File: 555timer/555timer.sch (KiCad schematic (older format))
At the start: 6 parts, among them SW1 SW_Push, U1 NE555

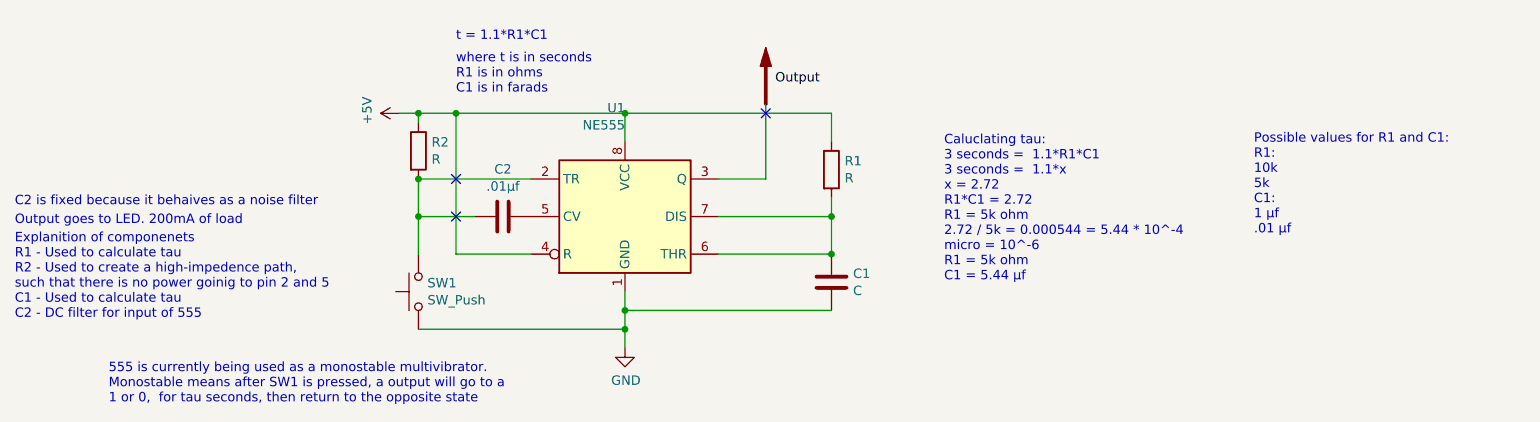
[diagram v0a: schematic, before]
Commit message: :recycle: Removing noise from schematic
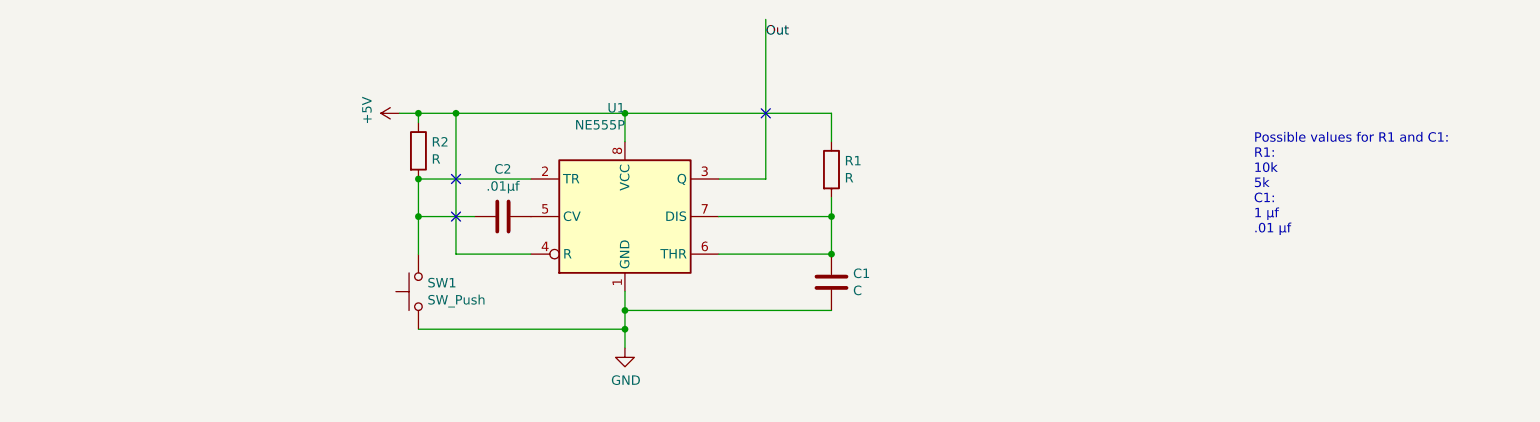
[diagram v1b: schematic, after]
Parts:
- U1: value NE555 -> NE555P
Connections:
- net labels added: Out
- net labels removed: Output
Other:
- note removed: "555 is currently being used as a monostable multivibrator. \nMonostable means after SW1 is pressed, a output will go to a\n1 or 0, for tau seconds, then return to the opposite state"
- note removed: "C2 is fixed because it behaives as a noise filter"
- note removed: "Caluclating tau:\n3 seconds = 1.1*R1*C1\n3 seconds = 1.1*x\nx = 2.72\nR1*C1 = 2.72\nR1 = 5k ohm\n2.72 / 5k = 0.000544 = 5.44 * 10^-4\nmicro = 10^-6\nR1 = 5k ohm\nC1 = 5.44 μf\n"
- note removed: "Explanition of componenets\nR1 - Used to calculate tau\nR2 - Used to create a high-impedence path,\nsuch that there is no power goinig to pin 2 and 5 \nC1 - Used to calculate tau\nC2 - DC filter for input of 555\n"
- note removed: "Output goes to LED. 200mA of load"
- note removed: "t = 1.1*R1*C1\n\n"
- note removed: "where t is in seconds\nR1 is in ohms\nC1 is in farads"
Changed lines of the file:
@@
 P 5000 3800
 F 0 "U1" H 5000 4378 50  0000 R CNN
-F 1 "NE555" H 5000 4287 50  0000 R CNN
+F 1 "NE555P" H 5000 4287 50  0000 R CNN
 F 2 "" H 5000 3800 50  0001 C CNN
 F 3 "http://www.ti.com/lit/ds/symlink/ne555.pdf" H 5000 3800 50  0001 C CNN
@@
 	6100 4000 5500 4000
 Connection ~ 6100 3800
-$Comp
-L Graphic:SYM_Arrow_Large #SYM?
-U 1 1 5C9155A3
-P 5750 3050
-F 0 "#SYM?" H 5750 3140 50  0001 C CNN
-F 1 "SYM_Arrow_Large" H 5750 2970 50  0001 C CNN
-F 2 "" H 5750 3050 50  0001 C CNN
-F 3 "~" H 5750 3050 50  0001 C CNN
-	1    5750 3050
-	0    -1   -1   0
-$EndComp
 Wire Wire Line
 	5500 3600 5750 3600
-Text Label 5800 3100 0    50   ~ 0
-Output
 $Comp
 L Device:R R2
@@
 Wire Wire Line
 	5000 3250 6100 3250
-Wire Wire Line
-	5750 3600 5750 3200
 Wire Wire Line
 	3900 3600 3900 3800
@@
 Wire Wire Line
 	3900 3800 3900 4000
-Text Notes 4100 2950 0    50   ~ 0
-t = 1.1*R1*C1\n\n
-Text Notes 4100 3150 0    50   ~ 0
-where t is in seconds\nR1 is in ohms\nC1 is in farads
-Text Notes 1750 3750 0    50   ~ 0
-C2 is fixed because it behaives as a noise filter
-Text Notes 1750 3850 0    50   ~ 0
-Output goes to LED. 200mA of load
-Text Notes 1750 4350 0    50   ~ 0
-Explanition of componenets\nR1 - Used to calculate tau\nR2 - Used to create a high-impedence path,\nsuch that there is no power goinig to pin 2 and 5 \nC1 - Used to calculate tau\nC2 - DC filter for input of 555\n
 NoConn ~ 5750 3250
 NoConn ~ 4100 3600
 NoConn ~ 4100 3800
-Text Notes 2250 4800 0    50   ~ 0
-555 is currently being used as a monostable multivibrator. \nMonostable means after SW1 is pressed, a output will go to a\n1 or 0,  for tau seconds, then return to the opposite state
-Text Notes 6700 4150 0    50   ~ 0
-Caluclating tau:\n3 seconds =  1.1*R1*C1\n3 seconds =  1.1*x\nx = 2.72\nR1*C1 = 2.72\nR1 = 5k ohm\n2.72 / 5k = 0.000544 = 5.44 * 10^-4\nmicro = 10^-6\nR1 = 5k ohm\nC1 = 5.44 μf\n
 Text Notes 8350 3900 0    50   ~ 0
 Possible values for R1 and C1:\nR1:\n10k\n5k\nC1:\n1 μf\n.01 μf
+Wire Wire Line
+	5750 2750 5750 3600
+Text Label 5750 2850 0    50   ~ 0
+Out
 $EndSCHEMATC

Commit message: :art: Updated Schematic for 555, now reflects most recent physical design
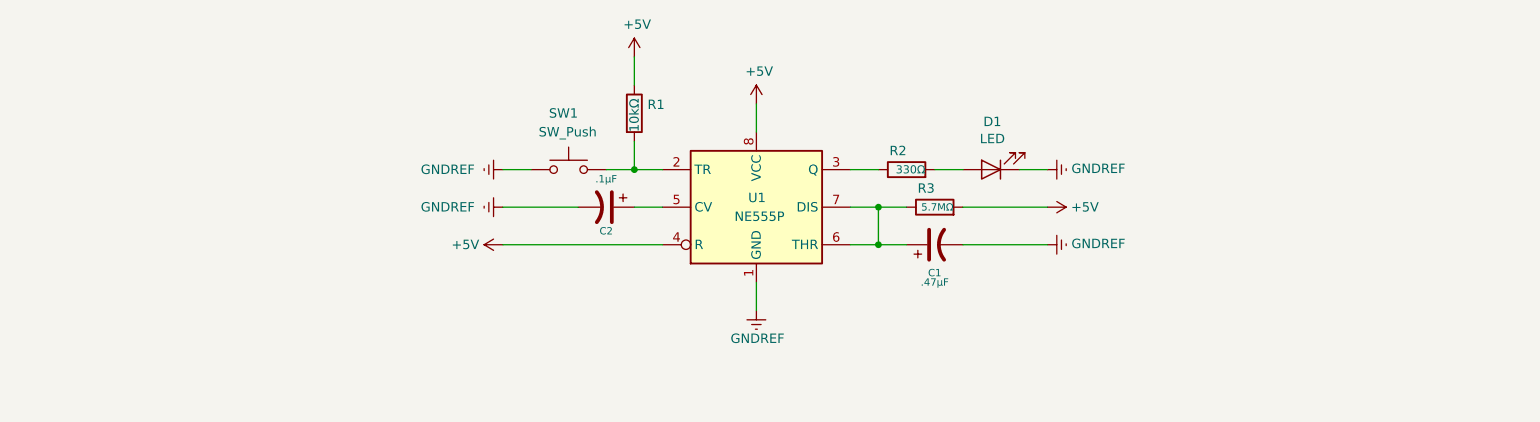
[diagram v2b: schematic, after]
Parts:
- removed C1: C, symbol Device:C
- removed C2: .01μf, symbol Device:C
- added C1: .47μF, symbol Device:CP1
- added C2: .1μF, symbol Device:CP1
- added D1: LED, symbol Device:LED
- added R3: 5.7MΩ, symbol Device:R
- R1: value R -> 10kΩ
- R2: value R -> 330Ω
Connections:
- net labels added: GNDREF
- net labels removed: GND, Out
- wire segments 24 -> 20
- no-connect marks 3 -> 0
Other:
- note removed: "Possible values for R1 and C1:\nR1:\n10k\n5k\nC1:\n1 μf\n.01 μf"
